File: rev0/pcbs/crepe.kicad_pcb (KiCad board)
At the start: 2 copper layers, 197.8 x 72 mm, 82 parts

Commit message: groundfill
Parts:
- added ?: , VIA-0.6mm, F.Cu at (-1.00, -26.8)
- added ?: , VIA-0.6mm, F.Cu at (1.00, -26.8)
- added PAD1: , SMDPad, F.Cu at (-1.00, -26.8)
- added PAD2: , SMDPad, F.Cu at (1.00, -26.8)
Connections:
- T1 pad 1: BAT- -> BAT
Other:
- outline, holes or cut-outs redrawn
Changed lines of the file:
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@@
 (net 46 "F1")
 (net 47 "F0")
-(net 48 "BAT-")
+(net 48 "BAT")
 (net 49 "mirror_pinky_extras")
 (net 50 "mirror_pinky_bottom")
@@
 (add_net "F1")
 (add_net "F0")
-(add_net "BAT-")
+(add_net "BAT")
 (add_net "mirror_pinky_extras")
 (add_net "mirror_pinky_bottom")
@@
             (pad "" np_thru_hole circle (at 1.5 0) (size 1 1) (drill 0.9) (layers *.Cu *.Mask))
             (pad "" np_thru_hole circle (at -1.5 0) (size 1 1) (drill 0.9) (layers *.Cu *.Mask))
-            (pad 1 smd rect (at 2.25 2.075 180) (size 0.9 1.25) (layers F.Cu F.Paste F.Mask) (net 48 "BAT-"))
+            (pad 1 smd rect (at 2.25 2.075 180) (size 0.9 1.25) (layers F.Cu F.Paste F.Mask) (net 48 "BAT"))
             (pad 2 smd rect (at -0.75 2.075 180) (size 0.9 1.25) (layers F.Cu F.Paste F.Mask) (net 31 "GND"))
             (pad 3 smd rect (at -2.25 2.075 180) (size 0.9 1.25) (layers F.Cu F.Paste F.Mask) )
@@
             (model "${KICAD6_3DMODEL_DIR}/Button_Switch_SMD.3dshapes/SW_SPDT_PCM12.wrl" (offset(xyz 0 0 0)) (scale(xyz 1 1 1)) (rotate(xyz 0 0 180)) )
         )
+        (module SMDPad (layer F.Cu)
+            (at -1 -26.75 90)
+            (fp_text reference "PAD1" (at 0 0) (layer F.SilkS) hide (effects (font (size 1.27 1.27) (thickness 0.15))))
+            (fp_text value "" (at 0 0) (layer F.SilkS) hide (effects (font (size 1.27 1.27) (thickness 0.15))))
+            (pad 1 smd rect (at 0 0 90) (size 2 1) (layers F.Cu F.Paste F.Mask) (net 30 "RAW"))
+(fp_text user + (at -2 0 90) (layer F.SilkS) (effects (font (size 0.8 0.8) (thickness 0.15)) ))
+        )
+      (module VIA-0.6mm (layer F.Cu)
+      (at -1 -26.75 0)
+      (pad 1 thru_hole circle (at 0 0) (size 0.6 0.6) (drill 0.3) (layers *.Cu) (zone_connect 2) (net 30 "RAW"))
+      )
+        (module SMDPad (layer F.Cu)
+            (at 1 -26.75 90)
+            (fp_text reference "PAD2" (at 0 0) (layer F.SilkS) hide (effects (font (size 1.27 1.27) (thickness 0.15))))
+            (fp_text value "" (at 0 0) (layer F.SilkS) hide (effects (font (size 1.27 1.27) (thickness 0.15))))
+            (pad 1 smd rect (at 0 0 90) (size 2 1) (layers F.Cu F.Paste F.Mask) (net 48 "BAT"))
+(fp_text user - (at -2 0 90) (layer F.SilkS) (effects (font (size 0.8 0.8) (thickness 0.15)) ))
+        )
+      (module VIA-0.6mm (layer F.Cu)
+      (at 1 -26.75 0)
+      (pad 1 thru_hole circle (at 0 0) (size 0.6 0.6) (drill 0.3) (layers *.Cu) (zone_connect 2) (net 48 "BAT"))
+      )
     (module Kailh-PG1425-X-Switch (layer F.Cu)
       (at 177.5 0 0)
@@
 (gr_line (start -9.875 -62.625) (end 185.875 -62.625) (angle 90) (layer Edge.Cuts) (width 0.15))
 (gr_line (start 186.875 -61.625) (end 186.875 8.375) (angle 90) (layer Edge.Cuts) (width 0.15))
-(gr_line (start 4.972683766666666 9.375) (end 185.875 9.375) (angle 90) (layer Edge.Cuts) (width 0.15))
-(gr_line (start 4.140633466666666 8.9297002) (end 3.734366533333333 8.3202998) (angle 90) (layer Edge.Cuts) (width 0.15))
-(gr_line (start 2.902316233333334 7.875) (end -2.902316233333334 7.875) (angle 90) (layer Edge.Cuts) (width 0.15))
-(gr_line (start -3.734366533333334 8.3202998) (end -4.140633466666667 8.929700200000001) (angle 90) (layer Edge.Cuts) (width 0.15))
-(gr_line (start -4.972683766666667 9.375) (end -9.875 9.375) (angle 90) (layer Edge.Cuts) (width 0.15))
+(gr_line (start 5.972683766666666 9.375) (end 185.875 9.375) (angle 90) (layer Edge.Cuts) (width 0.15))
+(gr_line (start 5.140633466666666 8.9297002) (end 4.734366533333333 8.320299799999997) (angle 90) (layer Edge.Cuts) (width 0.15))
+(gr_line (start 3.9023162333333343 7.875) (end -3.9023162333333334 7.875) (angle 90) (layer Edge.Cuts) (width 0.15))
+(gr_line (start -4.734366533333334 8.3202998) (end -5.140633466666666 8.9297002) (angle 90) (layer Edge.Cuts) (width 0.15))
+(gr_line (start -5.972683766666667 9.375) (end -9.875 9.375) (angle 90) (layer Edge.Cuts) (width 0.15))
 (gr_arc (start -9.875 -61.625) (end -9.875 -62.625) (angle -90) (layer Edge.Cuts) (width 0.15))
 (gr_arc (start 185.875 -61.625) (end 186.875 -61.625) (angle -90) (layer Edge.Cuts) (width 0.15))
 (gr_arc (start 185.875 8.375) (end 185.875 9.375) (angle -90) (layer Edge.Cuts) (width 0.15))
-(gr_arc (start 4.972683766666666 8.375) (end 4.140633466666666 8.9297002) (angle -56.30993247402026) (layer Edge.Cuts) (width 0.15))
-(gr_arc (start 2.902316233333334 8.875) (end 3.734366533333334 8.3202998) (angle -56.30993247402025) (layer Edge.Cuts) (width 0.15))
-(gr_arc (start -2.902316233333334 8.875) (end -2.902316233333334 7.875) (angle -56.30993247402026) (layer Edge.Cuts) (width 0.15))
-(gr_arc (start -4.972683766666667 8.375) (end -4.972683766666667 9.375) (angle -56.309932474020115) (layer Edge.Cuts) (width 0.15))
+(gr_arc (start 5.972683766666666 8.375) (end 5.140633466666666 8.9297002) (angle -56.30993247402026) (layer Edge.Cuts) (width 0.15))
+(gr_arc (start 3.9023162333333343 8.875) (end 4.7343665333333345 8.3202998) (angle -56.30993247402004) (layer Edge.Cuts) (width 0.15))
+(gr_arc (start -3.9023162333333334 8.875) (end -3.9023162333333334 7.875) (angle -56.30993247402026) (layer Edge.Cuts) (width 0.15))
+(gr_arc (start -5.972683766666667 8.375) (end -5.972683766666667 9.375) (angle -56.309932474020286) (layer Edge.Cuts) (width 0.15))
 (gr_arc (start -9.875 8.375) (end -10.875 8.375) (angle -90) (layer Edge.Cuts) (width 0.15))
 )

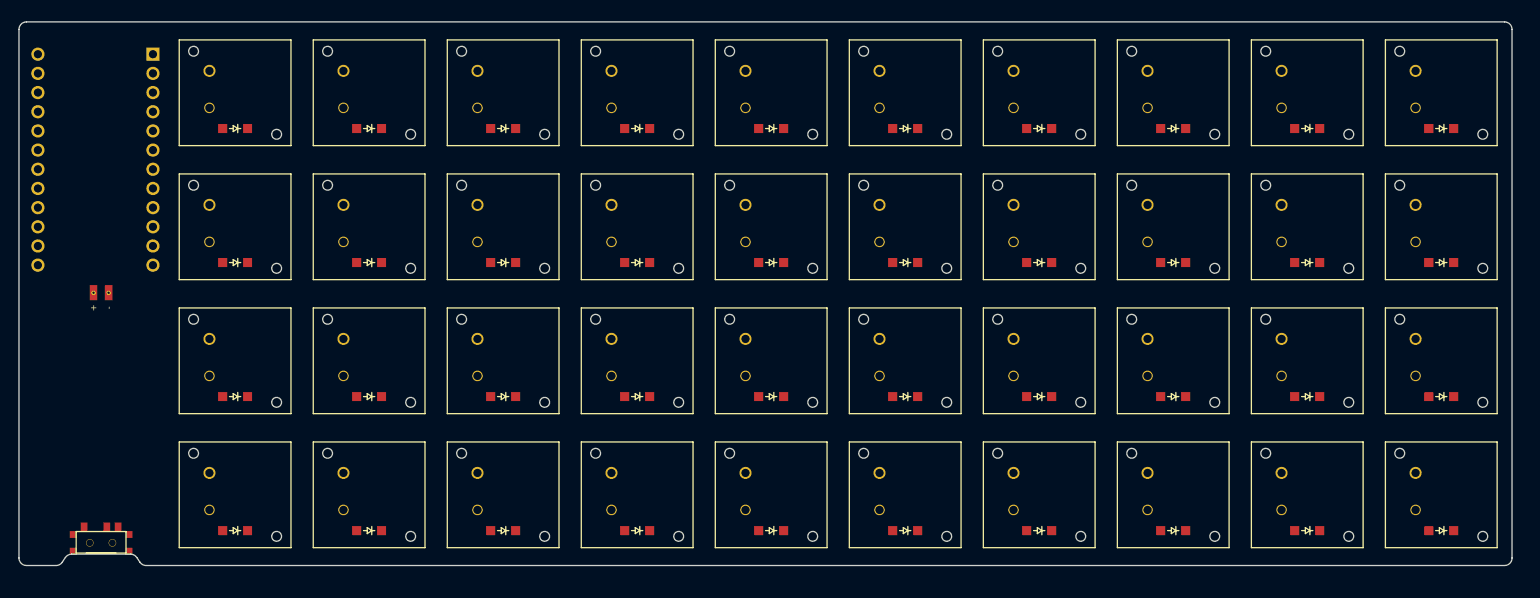
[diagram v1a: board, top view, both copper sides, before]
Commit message: forgot to save the kicad file
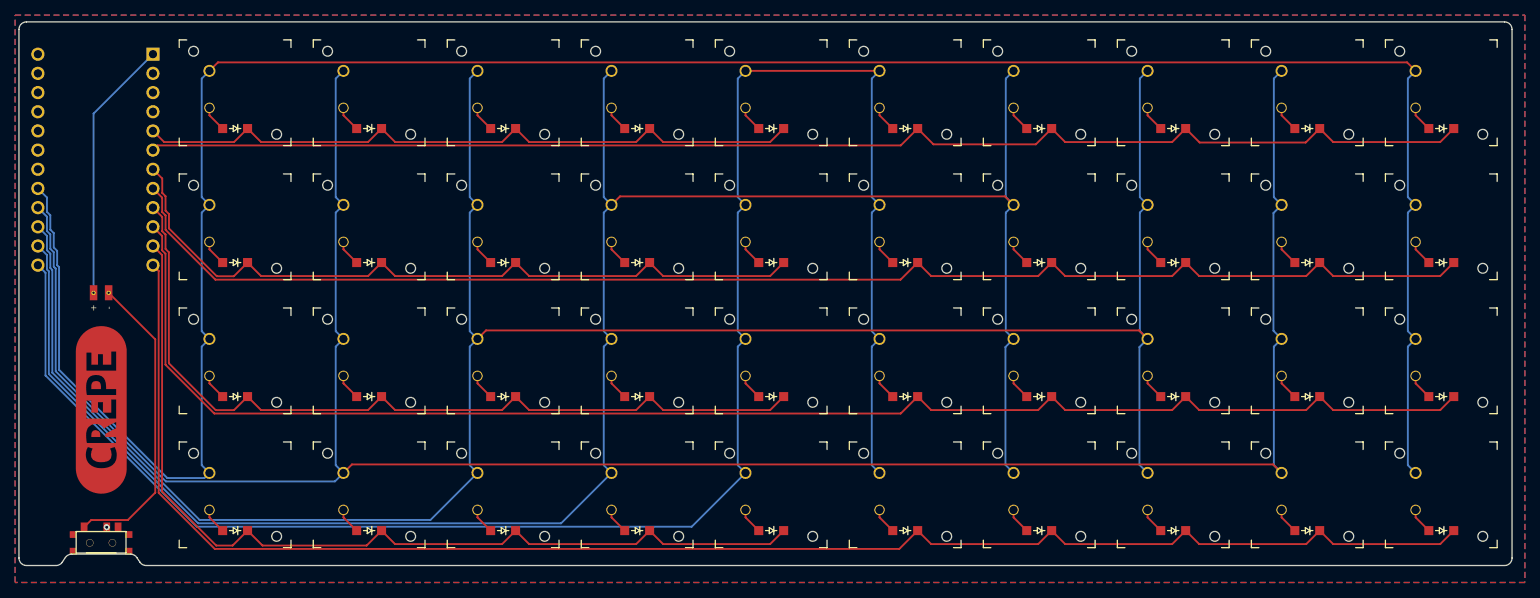
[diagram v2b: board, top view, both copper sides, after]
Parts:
- added kibuzzard-63705176: G***, kibuzzard-63705176, F.Cu at (0.03, -11.2)
- S1, S10, S11, S12, S13, S14, S15, S16, S17, S18, S19, S2, S20, S21, S22, S23, S24, S25, S26, S27, S28, S29, S3, S30, S31, S32, S33, S34, S35, S36, S37, S38, S39, S4, S40, S5, S6, S7, S8, S9: footprint Kailh-PG1425-X-Switch -> 0-jasonhazel-footprints:Kailh-PG1425-X-Switch
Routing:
- net c0: track 0.00 -> 323.6 mm
- net c1: track 0.00 -> 304.1 mm
- net c2: track 0.00 -> 288.4 mm
- net c3: track 0.00 -> 268.8 mm
- net c4: track 0.00 -> 248.3 mm
- net r7: track 0.00 -> 212.0 mm
- net r6: track 0.00 -> 199.1 mm
- net r5: track 0.00 -> 186.4 mm
- net r4: track 0.00 -> 179.7 mm
- net r3: track 0.00 -> 125.2 mm
- net r2: track 0.00 -> 112.1 mm
- net r1: track 0.00 -> 99.4 mm
- net r0: track 0.00 -> 90.8 mm
- net BAT: track 0.00 -> 40.4 mm
- net RAW: track 0.00 -> 34.9 mm
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- added copper zone on B.Cu, net GND
- added copper zone on F.Cu, net GND
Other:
- net class Default removed
